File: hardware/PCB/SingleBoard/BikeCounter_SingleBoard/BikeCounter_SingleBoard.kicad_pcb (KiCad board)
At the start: 2 copper layers, 122 x 122 mm, 23 parts, among them J1 PIR Sensor, J2 PIR Sensor 2, J3 Conn_01x02_Socket, J4 AM2320, SW1 SW_SPST, SW2 SW_DIP_x03

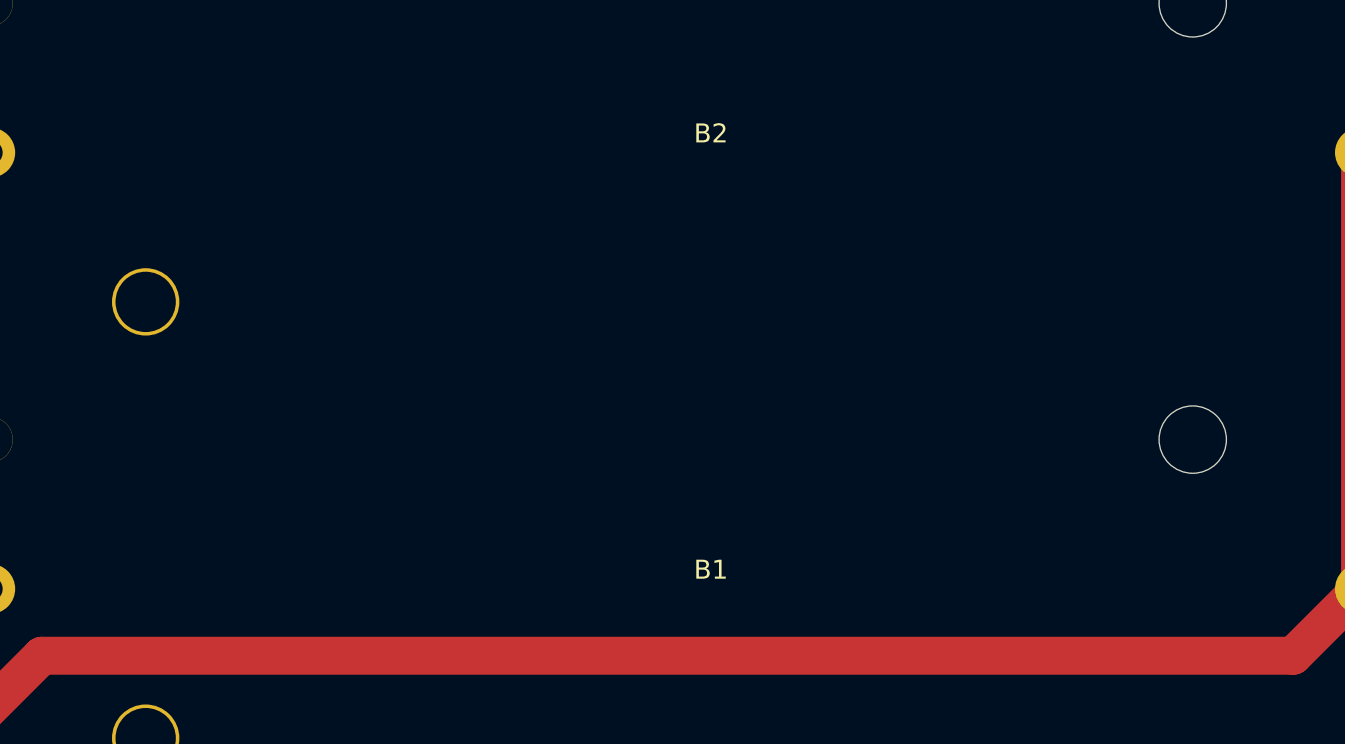
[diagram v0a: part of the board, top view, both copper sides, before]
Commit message: BOM finished
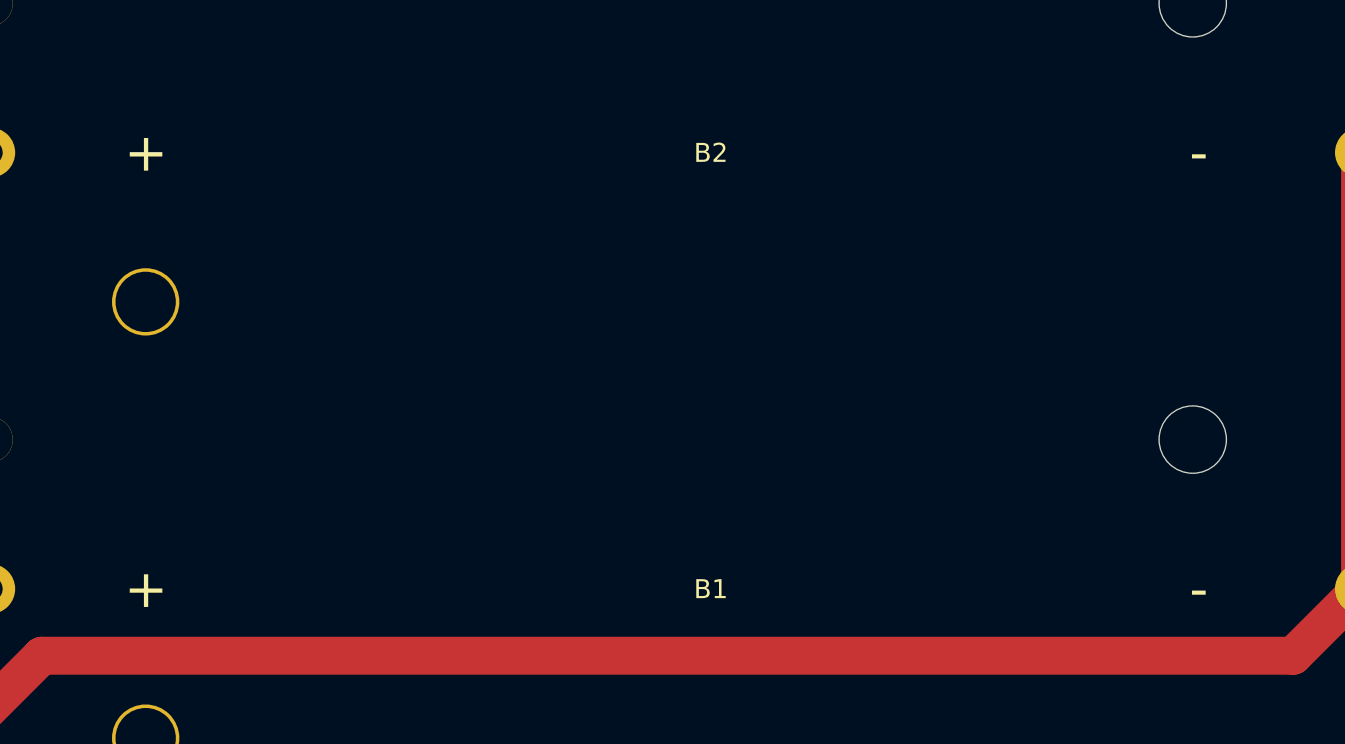
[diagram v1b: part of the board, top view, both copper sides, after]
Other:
- board text added: "+"
- board text added: "-"
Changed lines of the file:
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@@
 		(at 64.78 52.475 180)
 		(property "Reference" "B2"
-			(at -38 1 180)
+			(at -38 -0.025 180)
 			(layer "F.SilkS")
 			(effects
@@
 		(at 64.78 75.475 180)
 		(property "Reference" "B1"
-			(at -38 1 180)
+			(at -38 -0.025 180)
 			(layer "F.SilkS")
 			(effects
@@
 		)
 	)
+	(gr_text "+"
+		(at 73 52.5 0)
+		(layer "F.SilkS")
+		(effects
+			(font
+				(size 2 2)
+				(thickness 0.15)
+			)
+		)
+	)
 	(gr_text "debug"
 		(at 42.27 137.04 0)
@@
 		)
 	)
+	(gr_text "+"
+		(at 73 75.5 0)
+		(layer "F.SilkS")
+		(effects
+			(font
+				(size 2 2)
+				(thickness 0.15)
+			)
+		)
+	)
 	(gr_text "PIR2"
 		(at 116 148 0)
@@
 				(thickness 0.15)
 			)
+		)
+	)
+	(gr_text "-"
+		(at 128.5 52.5 0)
+		(layer "F.SilkS")
+		(effects
+			(font
+				(size 2 2)
+				(thickness 0.15)
+			)
+		)
+	)
+	(gr_text "-"
+		(at 128.5 75.5 0)
+		(layer "F.SilkS")
+		(effects
+			(font
+				(size 2 2)
+				(thickness 0.15)
+			)
